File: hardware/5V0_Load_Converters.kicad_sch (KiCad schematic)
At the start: 73 parts, among them J19 61300311121, Q26 EPC2016C, Q27 EPC2016C, Q8 SI2302DDS-T1-GE3, U21 INA199C3DCKR, U30 LTC3833EUDC-TRPBF

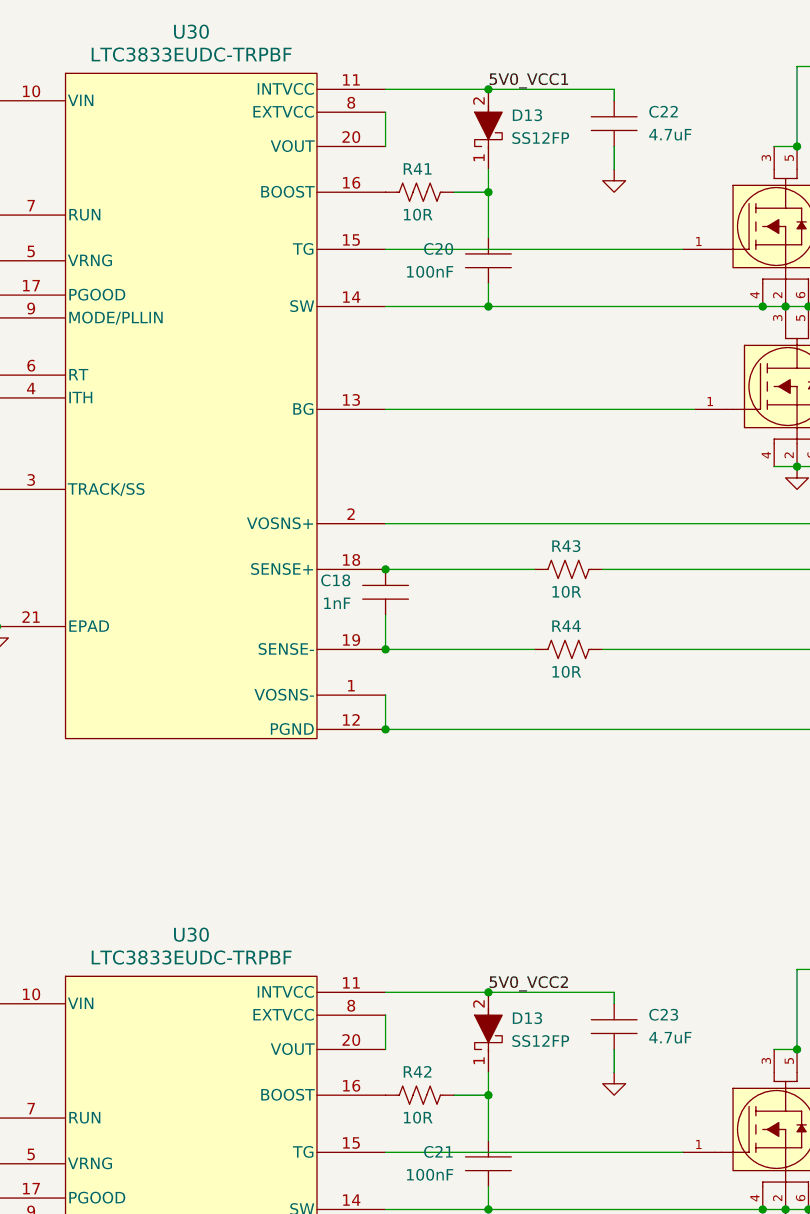
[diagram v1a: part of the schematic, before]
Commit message: hardware: Updating some zones in the layout and making minor changes in the schematic.
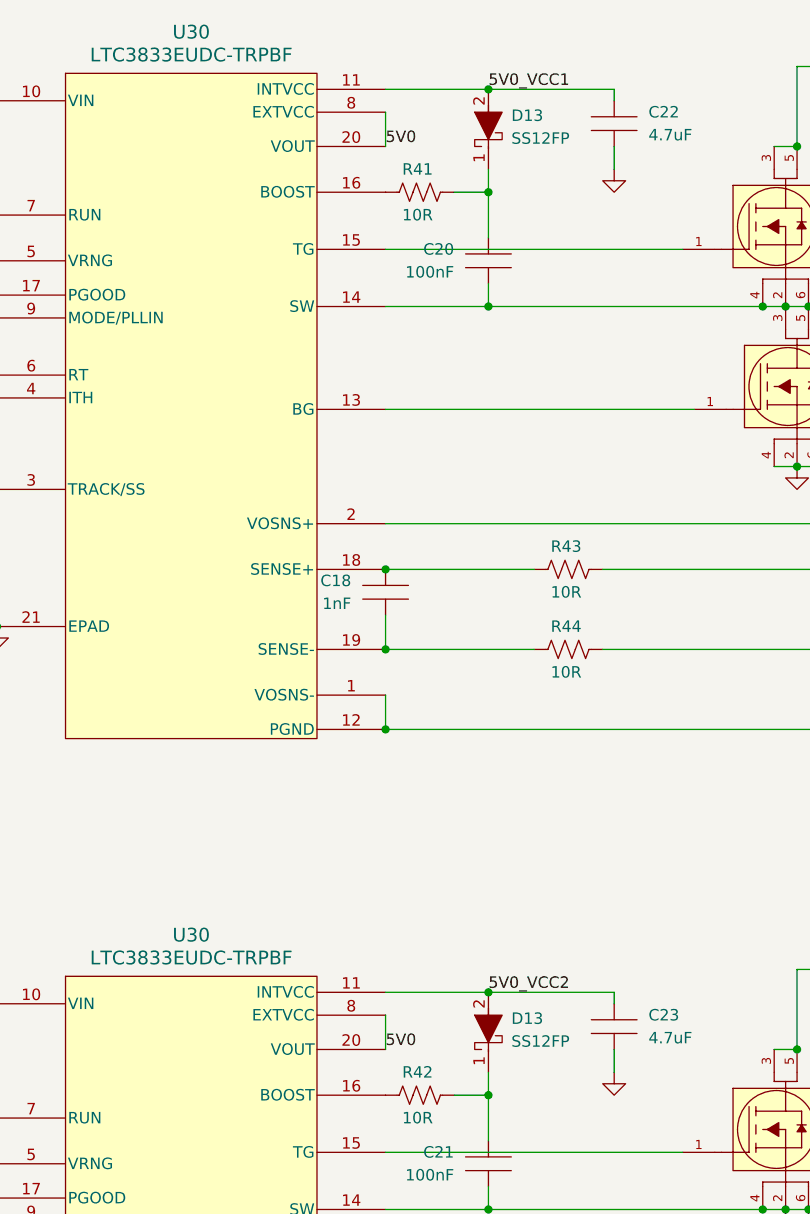
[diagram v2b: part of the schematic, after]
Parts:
- J19: footprint footprints:61300311121 -> footprints:three_position_jumper
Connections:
- net 5V0: now also U30.20 (VOUT), U30.20 (VOUT), U30.8 (EXTVCC), U30.8 (EXTVCC)
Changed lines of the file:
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@@
     (effects (font (size 1.27 1.27)) (justify left bottom))
   )
+  (label "5V0" (at 245.11 130.81 0) (fields_autoplaced)
+    (effects (font (size 1.27 1.27)) (justify left bottom))
+  )
   (label "5V0_VCC2" (at 134.62 147.32 0) (fields_autoplaced)
     (effects (font (size 1.27 1.27)) (justify left bottom))
   )
+  (label "5V0" (at 245.11 30.48 0) (fields_autoplaced)
+    (effects (font (size 1.27 1.27)) (justify left bottom))
+  )
   (label "5V0_VCC1" (at 134.62 46.99 0) (fields_autoplaced)
     (effects (font (size 1.27 1.27)) (justify left bottom))
@@
       (effects (font (size 1.27 1.27)) (justify left))
     )
-    (property "Footprint" "footprints:61300311121" (at 134.62 186.36 0)
+    (property "Footprint" "footprints:three_position_jumper" (at 134.62 186.36 0)
       (effects (font (size 1.27 1.27)) (justify left top) hide)
     )
@@
       (effects (font (size 1.27 1.27)) (justify left))
     )
-    (property "Footprint" "footprints:61300311121" (at 134.62 86.03 0)
+    (property "Footprint" "footprints:three_position_jumper" (at 134.62 86.03 0)
       (effects (font (size 1.27 1.27)) (justify left top) hide)
     )

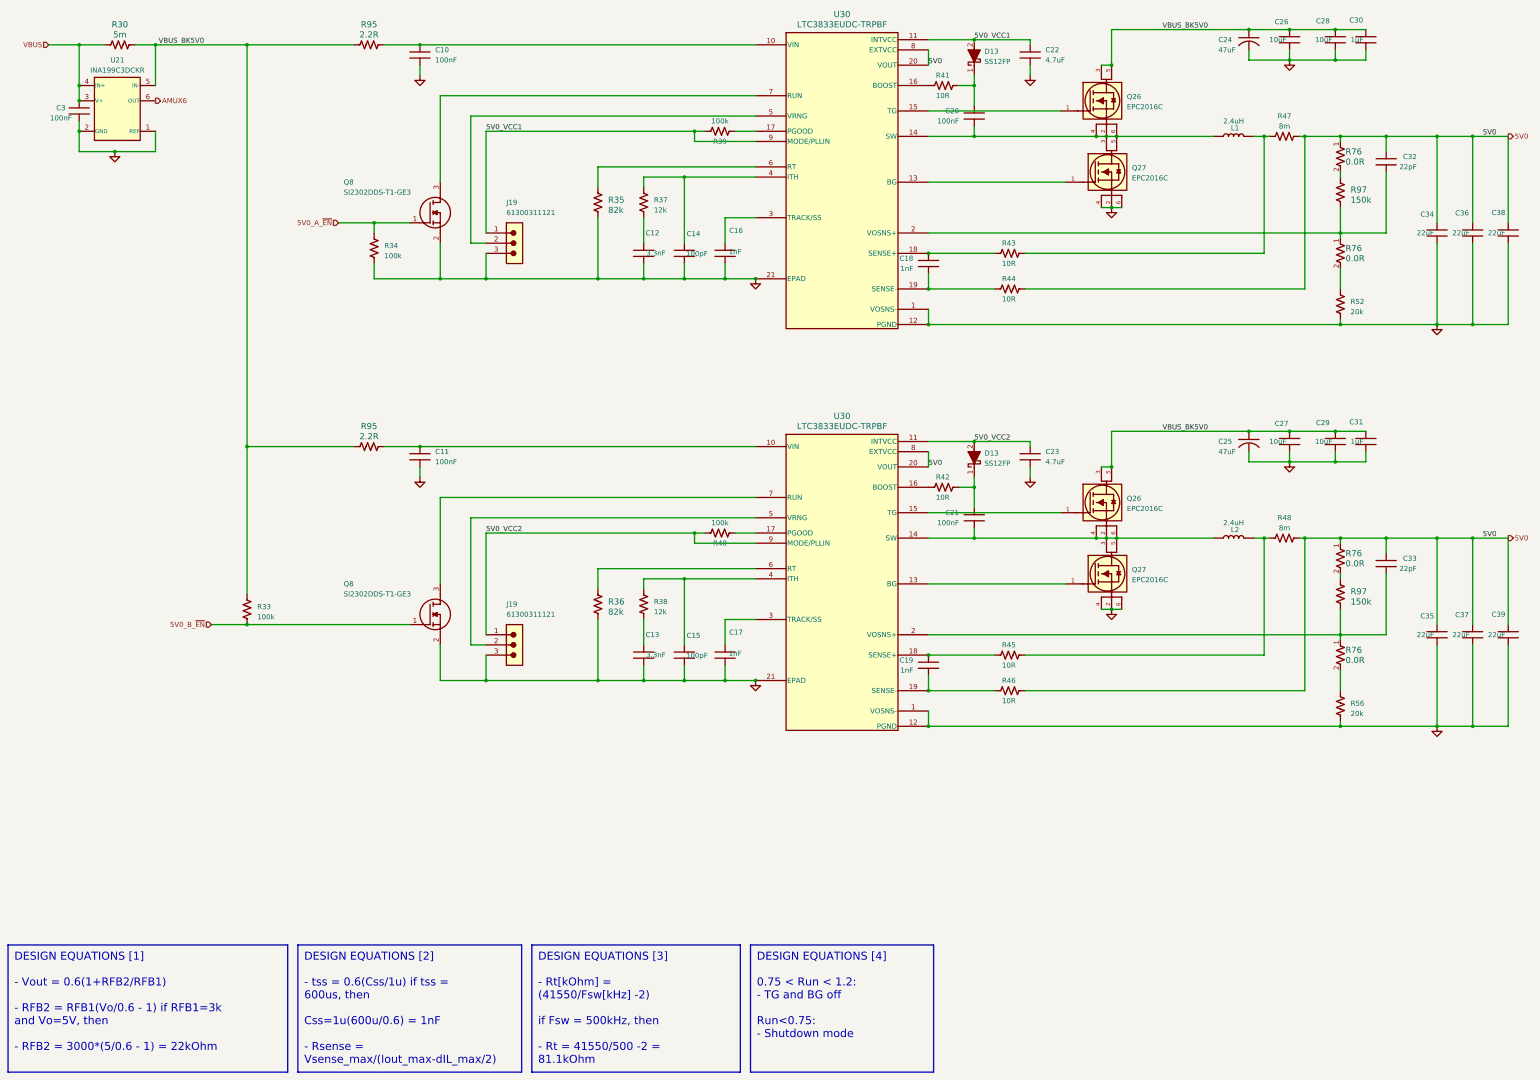
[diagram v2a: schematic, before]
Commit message: hardware: Updating the schematic and layout to solve #8, #9 and #10.
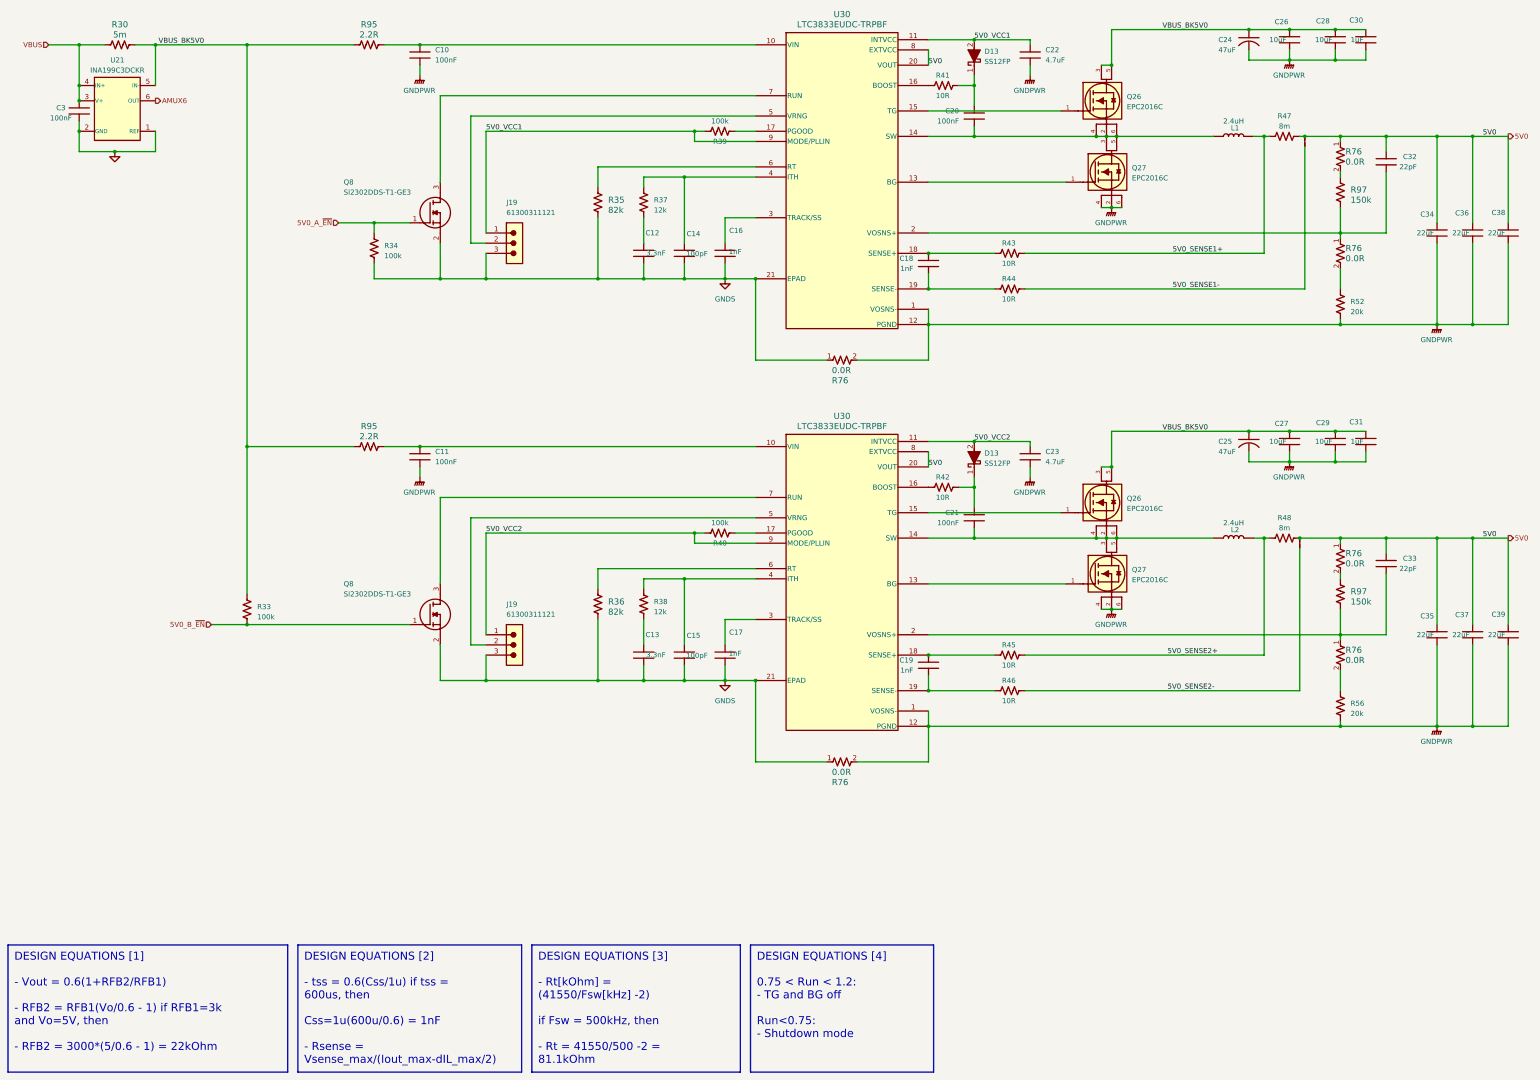
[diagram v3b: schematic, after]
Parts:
- added JP1, JP2: SolderJumper_2_Bridged, footprints:Jumper, symbol Jumper:Jumper
- added R76 (x2): 0.0R, footprints:CRCW06030000Z0EAHP, symbol CRCW06030000Z0EAHP:CRCW06030000Z0EAHP
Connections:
- net 5V0: now also JP1.2 (B), JP2.2 (B); no longer R44.1, R46.1
- net GND: no longer C10.1, C11.1, C12.2, C13.2, C14.2, C15.2, C16.2, C17.2, C22.2, C23.2, C24.1 (CATHODE), C25.1 (CATHODE), C26.2, C27.2, C28.2, C29.2, C30.2, C31.2, C34.1, C35.1, C36.1, C37.1, C38.1, C39.1, J19.3, J19.3, Q27.2 (Substrate), Q27.2 (Substrate), Q27.4 (Source), Q27.4 (Source), Q27.6 (Source), Q27.6 (Source), Q8.2 (S), Q8.2 (S), R34.1, R35.1, R36.1, R52.1, R56.1, U30.1 (VOSNS-), U30.1 (VOSNS-), U30.12 (PGND), U30.12 (PGND), U30.21 (EPAD), U30.21 (EPAD)
- net 5V0_SENSE1+: now reaches L1.2, R43.1, R47.2
- net 5V0_SENSE2+: now reaches L2.2, R45.1, R48.2
- new net 5V0_SENSE1-: JP2.1 (A), R44.1
- new net 5V0_SENSE2-: JP1.1 (A), R46.1
- new net GNDPWR: C10.1, C11.1, C22.2, C23.2, C24.1 (CATHODE), C25.1 (CATHODE), C26.2, C27.2, C28.2, C29.2, C30.2, C31.2, C34.1, C35.1, C36.1, C37.1, C38.1, C39.1, Q27.2 (Substrate), Q27.2 (Substrate), Q27.4 (Source), Q27.4 (Source), Q27.6 (Source), Q27.6 (Source), R52.1, R56.1, R76.2, R76.2, U30.1 (VOSNS-), U30.1 (VOSNS-), U30.12 (PGND), U30.12 (PGND)
- new net GNDS: C12.2, C13.2, C14.2, C15.2, C16.2, C17.2, J19.3, J19.3, Q8.2 (S), Q8.2 (S), R34.1, R35.1, R36.1, R76.1, R76.1, U30.21 (EPAD), U30.21 (EPAD)

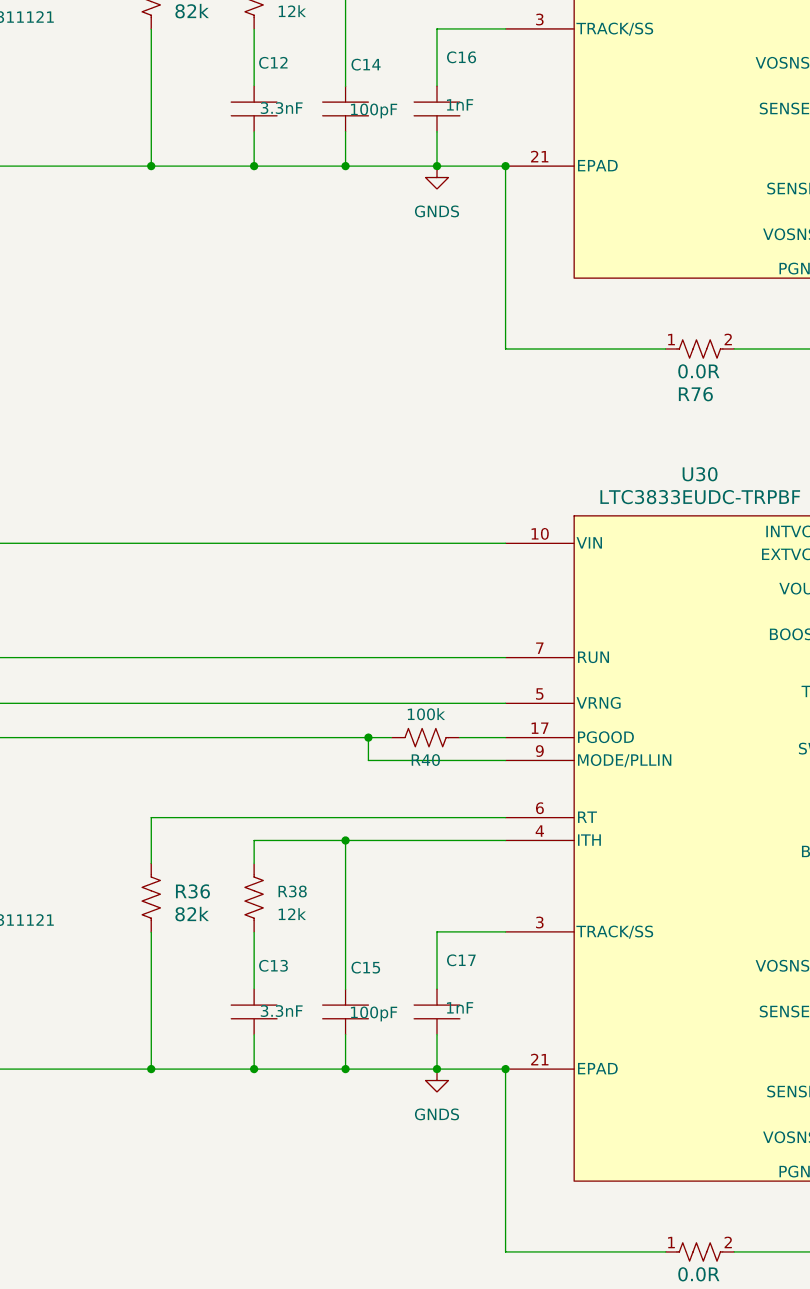
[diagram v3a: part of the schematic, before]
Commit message: hardware: Making corrections regarding #15, #14, #13 and starting #12 and #11.
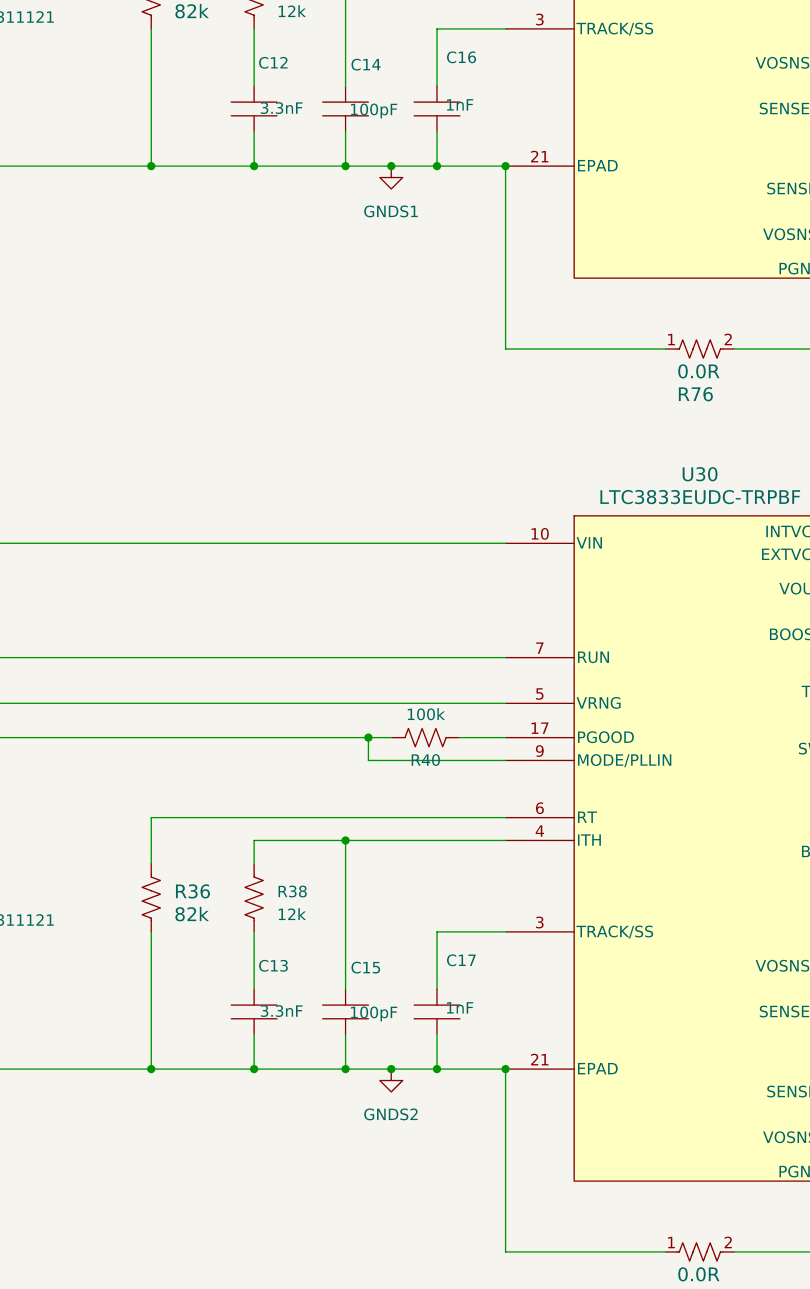
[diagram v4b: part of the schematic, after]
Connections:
- net GNDS renamed GNDS1
- net GNDS1: no longer C13.2, C15.2, C17.2, J19.3, Q8.2 (S), R36.1, R76.1, U30.21 (EPAD)
- new net GNDS2: C13.2, C15.2, C17.2, J19.3, Q8.2 (S), R36.1, R76.1, U30.21 (EPAD)
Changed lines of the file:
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@@
   (junction (at 41.91 52.07) (diameter 0) (color 0 0 0 0)
   )
+  (junction (at 189.23 184.15) (diameter 0) (color 0 0 0 0)
+  )
   (junction (at 256.54 135.89) (diameter 0) (color 0 0 0 0)
   )
@@
   (junction (at 162.56 184.15) (diameter 0) (color 0 0 0 0)
   )
+  (junction (at 189.23 83.82) (diameter 0) (color 0 0 0 0)
+  )
   (junction (at 256.54 24.13) (diameter 0) (color 0 0 0 0)
   )
@@
     (stroke (width 0) (type default))
   )
-  (wire (pts (xy 184.15 184.15) (xy 194.31 184.15))
+  (wire (pts (xy 184.15 184.15) (xy 189.23 184.15))
     (stroke (width 0) (type default))
   )
@@
     (stroke (width 0) (type default))
   )
+  (wire (pts (xy 189.23 83.82) (xy 194.31 83.82))
+    (stroke (width 0) (type default))
+  )
   (wire (pts (xy 288.29 130.81) (xy 290.83 130.81))
     (stroke (width 1) (type default))
@@
     (stroke (width 0) (type default))
   )
-  (wire (pts (xy 184.15 83.82) (xy 194.31 83.82))
+  (wire (pts (xy 184.15 83.82) (xy 189.23 83.82))
     (stroke (width 0) (type default))
   )
@@
     (stroke (width 1) (type default))
   )
+  (wire (pts (xy 189.23 184.15) (xy 194.31 184.15))
+    (stroke (width 0) (type default))
+  )
   (wire (pts (xy 201.93 104.14) (xy 201.93 83.82))
     (stroke (width 0) (type default))
@@
     )
   )
+  (symbol (lib_id "GNDS2:GNDS2") (at 189.23 184.15 0) (unit 1)
+    (in_bom yes) (on_board yes) (dnp no) (fields_autoplaced)
+    (property "Reference" "#PWR055" (at 189.23 190.5 0)
+      (effects (font (size 1.27 1.27)) hide)
+    )
+    (property "Value" "GNDS2" (at 189.23 189.23 0)
+      (effects (font (size 1.27 1.27)))
+    )
+    (property "Footprint" "" (at 189.23 184.15 0)
+      (effects (font (size 1.27 1.27)) hide)
+    )
+    (property "Datasheet" "" (at 189.23 184.15 0)
+      (effects (font (size 1.27 1.27)) hide)
+    )
+    (pin "1")
+    (instances
+      (project "eps-re_project"
+        (path "/2eebaa11-d7ed-4bfd-bc8e-988f68654d29/6cd5fe02-9b19-49bf-9109-b0a2c2f10c14"
+          (reference "#PWR055") (unit 1)
+        )
+      )
+    )
+  )
   (symbol (lib_id "61300311121:61300311121") (at 134.62 172.72 0) (unit 1)
     (in_bom yes) (on_board yes) (dnp no)
@@
     )
   )
-  (symbol (lib_id "power:GNDS") (at 194.31 184.15 0) (unit 1)
-    (in_bom yes) (on_board yes) (dnp no) (fields_autoplaced)
-    (property "Reference" "#PWR055" (at 194.31 190.5 0)
-      (effects (font (size 1.27 1.27)) hide)
-    )
-    (property "Value" "GNDS" (at 194.31 189.23 0)
-      (effects (font (size 1.27 1.27)))
-    )
-    (property "Footprint" "" (at 194.31 184.15 0)
-      (effects (font (size 1.27 1.27)) hide)
-    )
-    (property "Datasheet" "" (at 194.31 184.15 0)
-      (effects (font (size 1.27 1.27)) hide)
-    )
-    (pin "1")
-    (instances
-      (project "eps-re_project"
-        (path "/2eebaa11-d7ed-4bfd-bc8e-988f68654d29/6cd5fe02-9b19-49bf-9109-b0a2c2f10c14"
-          (reference "#PWR055") (unit 1)
-        )
-      )
-    )
-  )
   (symbol (lib_id "GCM32ER71C226KE19L:GCM32ER71C226KE19L") (at 389.89 170.18 0) (unit 1)
     (in_bom yes) (on_board yes) (dnp no)
@@
     )
   )
-  (symbol (lib_id "power:GNDS") (at 194.31 83.82 0) (unit 1)
-    (in_bom yes) (on_board yes) (dnp no) (fields_autoplaced)
-    (property "Reference" "#PWR052" (at 194.31 90.17 0)
-      (effects (font (size 1.27 1.27)) hide)
-    )
-    (property "Value" "GNDS" (at 194.31 88.9 0)
-      (effects (font (size 1.27 1.27)))
-    )
-    (property "Footprint" "" (at 194.31 83.82 0)
-      (effects (font (size 1.27 1.27)) hide)
-    )
-    (property "Datasheet" "" (at 194.31 83.82 0)
-      (effects (font (size 1.27 1.27)) hide)
-    )
-    (pin "1")
-    (instances
-      (project "eps-re_project"
-        (path "/2eebaa11-d7ed-4bfd-bc8e-988f68654d29/6cd5fe02-9b19-49bf-9109-b0a2c2f10c14"
-          (reference "#PWR052") (unit 1)
-        )
-      )
-    )
-  )
   (symbol (lib_id "power:GNDPWR") (at 372.11 195.58 0) (unit 1)
     (in_bom yes) (on_board yes) (dnp no) (fields_autoplaced)
@@
         )
       )
+    )
+  )
+  (symbol (lib_id "GNDS1:GNDS1") (at 189.23 83.82 0) (unit 1)
+    (in_bom yes) (on_board yes) (dnp no) (fields_autoplaced)
+    (property "Reference" "#PWR052" (at 189.23 90.17 0)
+      (effects (font (size 1.27 1.27)) hide)
+    )
+    (property "Value" "GNDS1" (at 189.23 88.9 0)
+      (effects (font (size 1.27 1.27)))
+    )
+    (property "Footprint" "" (at 189.23 83.82 0)
+      (effects (font (size 1.27 1.27)) hide)
+    )
+    (property "Datasheet" "" (at 189.23 83.82 0)
+      (effects (font (size 1.27 1.27)) hide)
+    )
+    (pin "1")
+    (instances
+      (project "eps-re_project"
+        (path "/2eebaa11-d7ed-4bfd-bc8e-988f68654d29/6cd5fe02-9b19-49bf-9109-b0a2c2f10c14"
+          (reference "#PWR052") (unit 1)
+        )
+      )
